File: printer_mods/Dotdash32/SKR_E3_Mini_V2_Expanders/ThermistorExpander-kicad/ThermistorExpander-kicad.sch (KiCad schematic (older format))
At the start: 8 parts, among them J1 SPI_Header, J2 JST-XH2, J3 JST-XH2, J4 JST-XH2

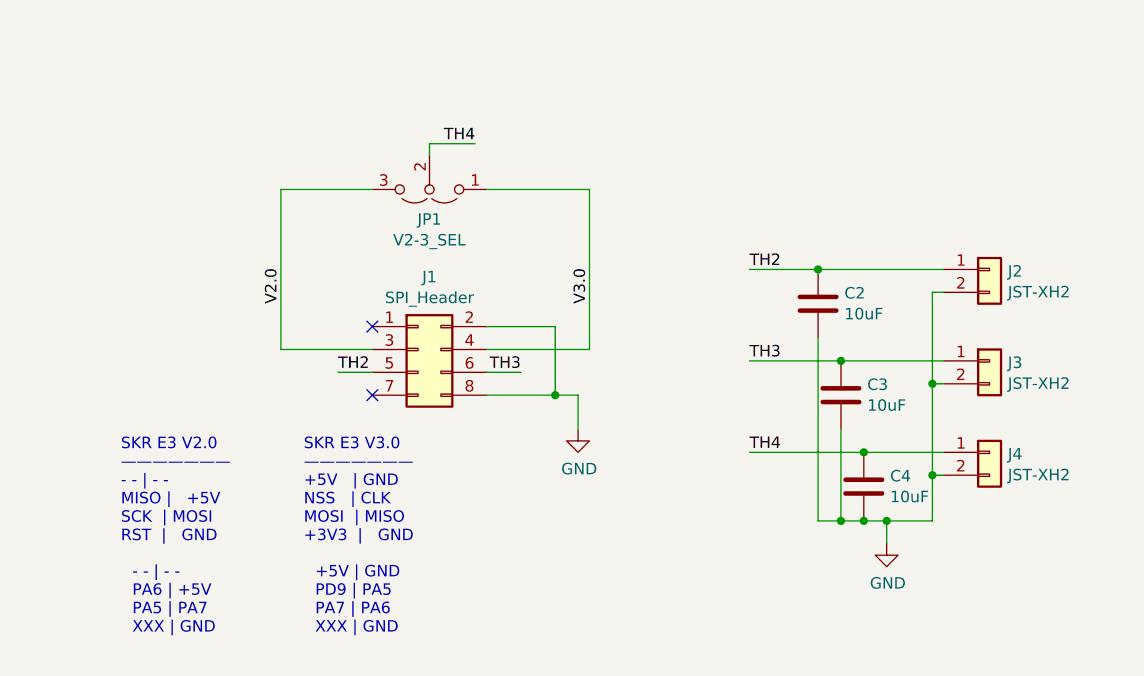
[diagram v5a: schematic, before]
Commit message: feat: updating BOM, add fiducials
JLCPCB 1206 caps are "discontinued" so moving to instock 0805
capacitors.  Updating BOM, creating LCSC importer
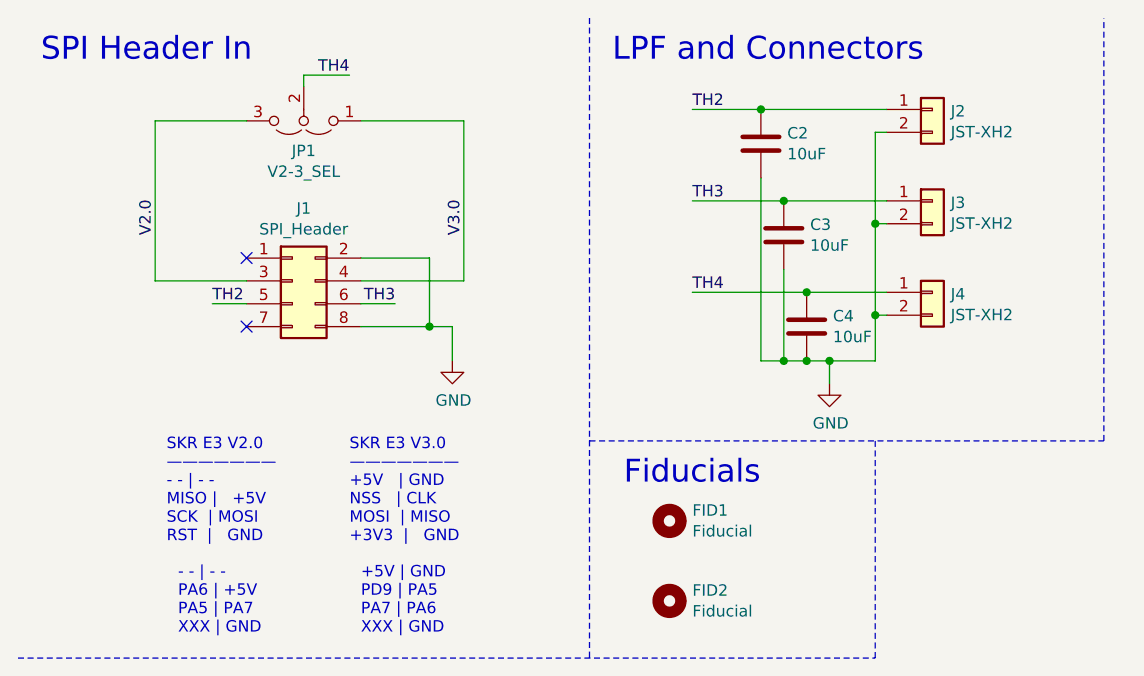
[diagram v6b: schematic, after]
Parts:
- added FID1, FID2: Fiducial, Fiducials:Fiducial_0.5mm_Dia_1mm_Outer, symbol Mechanical:MountingHole
- C2, C3, C4: footprint Capacitors_SMD:C_1206_HandSoldering -> Capacitors_SMD:C_0805_HandSoldering
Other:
- note added: "Fiducials"
- note added: "LPF and Connectors"
- note added: "SPI Header In"
- moved on the sheet: C2, C3, C4, J1, J2, J3, J4, JP1
